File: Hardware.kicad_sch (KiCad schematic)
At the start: 56 parts, among them J1 Conn_01x06_Socket, J2 Micro_SD_Card_Det1, Q1 BC849, Q2 BC849, SW1 Push_Button, SW2 Push_Button, U1 ESP32-WROOM-32, U2 LD1117S33TR_SOT223, U3 SN65HVD231, U4 74LVC125, U5 AMS1117CD-5.0, U6 AMS1117CD-3.3, U7 NEO-M8M, U8 LD1117S33TR_SOT223, U9 AT24CS01-XHM

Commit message: mostly finisged scematics
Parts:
- added AE2, AE3: Antenna_Shield, symbol Device:Antenna_Shield
- added C18, C21, C24: C, symbol Device:C
- added C19, C32, C33, C34: 0.1uF, symbol Device:C
- added C20: 0.1uF, Capacitor_SMD:C_0805_2012Metric_Pad1.18x1.45mm_HandSolder, symbol Device:C_Small
- added C25: 22pF, symbol Device:C
- added C26, C30: 100uF, symbol Device:C
- added C31: 1uF, symbol Device:C
- added D4: ESDA5V3SC5, Package_TO_SOT_SMD:SOT-23-5, symbol Power_Protection:ESDA5V3SC5
- added D5: BSD3C051V, Diode_SMD:D_SOD-323, symbol Device:D_TVS
- added D6, D7: LED, symbol Device:LED
- added D8: BAT54W, Package_TO_SOT_SMD:SOT-323_SC-70, symbol Diode:BAT54W
- added J3: SIM_Card_Shielded, symbol Connector:SIM_Card_Shielded
- added J5: USB_C_Receptacle_USB2.0_14P, symbol Connector:USB_C_Receptacle_USB2.0_14P
- added JP1: SolderJumper_2_Open, symbol Jumper:SolderJumper_2_Open
- added JP2: Jumper_2_Open, symbol Jumper:Jumper_2_Open
- added L2: BLM15PX121SN1D, Inductor_SMD:L_0402_1005Metric, symbol Device:L_Small
- added L3: blm18bb121sn1d, symbol Device:L_Ferrite
- added Q3, Q4, Q6: DTC143Z, symbol Transistor_BJT:DTC143Z
- added Q5: FDN340P, Package_TO_SOT_SMD:SOT-23, symbol Transistor_FET:FDN340P
- added R13: 1M, Resistor_SMD:R_1206_3216Metric_Pad1.30x1.75mm_HandSolder, symbol Device:R_Small
- added R14, R15: 5.1k, Resistor_SMD:R_1206_3216Metric_Pad1.30x1.75mm_HandSolder, symbol Device:R_Small
- added R16: 0R, symbol Device:R
- added R17, R18, R19, R20: R, symbol Device:R
- added U10: SIM7080G, SIM7080G:XCVR_SIM7080G, symbol SIM7080G:SIM7080G
- added U11: TXB0104PW, Package_SO:TSSOP-14_4.4x5mm_P0.65mm, symbol Logic_LevelTranslator:TXB0104PW
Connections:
- net 3.3V: now also C33.1, Q5.2 (S), R20.1, U10.34 (VBAT), U10.35 (VBAT), U11.14 (VCCB)
- net DTR: now also U11.3 (A2)
- net GND: now also AE2.2 (Shield), AE3.2 (Shield), C18.2, C19.2, C20.1, C21.2, C24.2, C26.2, C30.2, C31.2, C32.2, C33.2, C34.1, D4.2 (A), D5.2 (A2), J3.5 (GND), J3.SH, J5.S1 (SHIELD), JP2.1 (A), L2.2, Q3.2 (E), Q4.2 (E), Q6.2 (E), R13.1, U10.13 (GND), U10.19 (GND), U10.21 (GND), U10.27 (GND), U10.30 (GND), U10.31 (GND), U10.33 (GND), U10.36 (GND), U10.37 (GND), U10.45 (GND), U10.63 (GND), U10.66 (GND), U10.67 (GND), U10.69 (GND), U10.70 (GND), U10.71 (GND), U10.72 (GND), U10.73 (GND), U10.74 (GND), U10.75 (GND), U10.76 (GND), U10.77 (GND), U10.8 (GND), U11.7 (GND)
- new net: C21.1, R16.1, U10.32 (RF_ANT)
- new net: D8.1 (A), JP2.2 (B), U10.39 (PWRKEY)
- new net: J5.A5 (CC1), R14.1
- new net: JP1.1 (A), R19.2
- new net: AE2.1 (A), C24.1, R16.2
- new net: D7.1 (K), Q4.3 (C)
- new net: D7.2 (A), R18.2
- new net: Q5.1 (G), Q6.3 (C), R20.2
- new net: L3.2, Q5.3 (D)
- new net: J5.B5 (CC2), R15.1
- new net: D6.2 (A), R17.2
- new net: JP1.2 (B), U10.20 (USB_BOOT)
- new net: C25.2, U10.68 (GNSS_ANT)
- new net: D6.1 (K), Q3.3 (C)
- new net 1.8V: C34.2, R19.1, U10.40 (VDD_EXT), U11.1 (VCCA), U11.8 (OE)
- new net ANT_CTRL: Q6.1 (B)
- new net GNDPWR: C20.2, D5.1 (A1), J5.A1 (GND), J5.A12 (GND), J5.B1 (GND), J5.B12 (GND), L2.1, R13.2, R14.2, R15.2
- new net NB_RI: U10.7 (UART1_RI), U11.13 (B1)
- new net NB_RXD: U10.2 (UART1_RXD), U11.11 (B3)
- new net NB_TXD: U10.1 (UART1_TXD), U11.10 (B4)
- new net ND_DTR: U10.6 (UART1_DTR), U11.12 (B2)
- new net NETLIGHT: Q4.1 (B), U10.41 (NETLIGHT)
- new net PWRKEY: D8.3 (K)
- new net RI: U11.2 (A1)
- new net RXD: U11.4 (A3)
- new net SIM_CLK: D4.1 (K), J3.3 (CLK), U10.16 (SIM_CLK)
- new net SIM_DATA: D4.3 (K), J3.7 (I/O), U10.15 (SIM_DATA)
- new net SIM_RST: D4.4 (K), J3.2 (RST), U10.17 (SIM_RST)
- new net SIM_VDD: C18.1, D4.5 (K), J3.1 (VCC), U10.18 (SIM_VDD)
- new net STAT: Q3.1 (B), U10.42 (STATUS)
- new net TXD: U11.5 (A4)
- new net USB D+: J5.A6 (D+), J5.B6 (D+), U10.25 (USB_DP)
- new net USB D-: J5.A7 (D-), J5.B7 (D-), U10.26 (USB_DM)
- new net VANT: AE3.1 (A), C25.1, L3.1
- new net VBAT: C26.1, C30.1, C31.1, C32.1, R17.1, R18.1
- new net VBUS: C19.1, J5.A4 (VBUS), J5.A9 (VBUS), J5.B4 (VBUS), J5.B9 (VBUS), U10.24 (USB_VBUS)
- no-connect marks 33 -> 60
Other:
- note added: "LTE"
- moved on the sheet: AE1, BT1, C10, C11, C12, C13, C14, C15, C16, C17, C2, C22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

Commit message: done some layouting
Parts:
- removed C10, C15, C2, C3: 100nF, symbol Device:C
- removed C11, C12, C16, C8: 10uF, Capacitor_SMD:C_1206_3216Metric_Pad1.33x1.80mm_HandSolder, symbol Device:C
- removed C13, C14, C17, C9: 4.7uF, symbol Device:C
- removed U2, U8: LD1117S33TR_SOT223, Package_TO_SOT_SMD:SOT-223-3_TabPin2, symbol Regulator_Linear:LD1117S33TR_SOT223
- removed U5: AMS1117CD-5.0, Package_TO_SOT_SMD:TO-252-3_TabPin2, symbol Regulator_Linear:AMS1117CD-5.0
- removed U6: AMS1117CD-3.3, Package_TO_SOT_SMD:TO-252-3_TabPin2, symbol Regulator_Linear:AMS1117CD-3.3
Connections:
- net 3.3v is gone; now on net +3.3V: D2.2 (A), U7.23 (VCC), U9.8 (VCC)
- net CanH_Out is gone; now on net CanH: C27.2, D3.2, L4.3, R10.2
- net CanL_Out is gone; now on net CanL: C29.2, D3.1, L4.4, R11.2
- net Gps_RX is gone; now on net GPS_RX: U7.21 (RXD/SPI_MOSI)
- net Gps_TX is gone; now on net GPS_TX: U7.20 (TXD/SPI_MISO)
- net RXD is gone; now on net LTE_RX: U11.4 (A3)
- net TXD is gone; now on net LTE_TX: U11.5 (A4)
- net VBAT is gone; now on net +3.3V: C26.1, C30.1, C31.1, C32.1, R17.1, R18.1
- net ANT_CTRL: now also U1.11 (IO26)
- net CanH: no longer L4.2, U3.7 (CANH)
- net CanL: no longer L4.1, U3.6 (CANL)
- net PWRKEY: now also U1.10 (IO25)
- net LTE_RX: now reaches U1.16 (IO13)
- net LTE_TX: now reaches U1.27 (IO16)
- net GPS_RX: now reaches U1.28 (IO17)
- net GPS_TX: now reaches U1.33 (IO21)
- net 3.3V renamed +3.3V
- net CS_SD renamed SD_CS
- net Gps_SCL renamed GPS_SCL
- net Gps_SDA renamed GPS_SDA
- net RX renamed PROG_RX
- net RxCan renamed CAN_RX
- net TX renamed PROG_TX
- net TxCan renamed CAN_TX
- new net CanH_Int: L4.2, U3.7 (CANH)
- new net CanL_Int: L4.1, U3.6 (CANL)
- no-connect marks 60 -> 55
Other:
- note added: "GSM antenna controll"
- note added: "LTE Info Leds"
- note added: "LTE Module"
- note added: "LTE Usb"
- note added: "Levelshifter for LTE"
- note added: "SIM Card"
- note removed: "LTE"
- note removed: "Voltage Converter"
- moved on the sheet: AE2, AE3, BT1, C1, C18, C19, C20, C21, C22, C23, C24, C25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

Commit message: added testpoints
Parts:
- added H1, H2, H3, H4, H5, H6, H7, H8: MountingHole_Pad, symbol Mechanical:MountingHole_Pad
- added TP1, TP10, TP11, TP12, TP13, TP14, TP15, TP16, TP17, TP3, TP4, TP5, TP6, TP7, TP8, TP9: TestPoint, symbol Connector:TestPoint
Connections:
- net +3.3V: now also TP4.1
- net +3V3: now also TP17.1
- net ANT_CTRL: now also TP10.1
- net CAN_RX: now also TP14.1
- net CAN_TX: now also TP13.1
- net CanH_Int: now also TP12.1
- net CanL_Int: now also TP11.1
- net EN: now also TP15.1
- net GND: now also H1.1, H2.1, H3.1, H4.1, H5.1, H6.1, H7.1, H8.1
- net IO0: now also TP16.1
- net NETLIGHT: now also TP8.1
- net STAT: now also TP9.1
- net USB D+: now also TP7.1
- net USB D-: now also TP6.1
- net VANT: now also TP3.1
- net at D8.1 (A), JP2.2 (B), U10.39 (PWRKEY): now also TP5.1
- no-connect marks 55 -> 53
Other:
- note added: "Mounting"
- moved on the sheet: AE2, AE3, C1, C19, C21, C24, C25, C26, C27, C28, C29, C30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

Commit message: moved everythint into hirachical sheets
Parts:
- removed AE1: Antenna, symbol Device:Antenna
- removed AE2, AE3: Antenna_Shield, symbol Device:Antenna_Shield
- removed BT1: Battery_Cell, symbol Device:Battery_Cell
- removed C18, C21, C24: C, symbol Device:C
- removed C19, C32, C33, C34: 0.1uF, symbol Device:C
- removed C20: 0.1uF, Capacitor_SMD:C_0805_2012Metric_Pad1.18x1.45mm_HandSolder, symbol Device:C_Small
- removed C25: 22pF, symbol Device:C
- removed C26, C30: 100uF, symbol Device:C
- removed C27, C29: 100pF, Capacitor_SMD:C_0805_2012Metric_Pad1.18x1.45mm_HandSolder, symbol Device:C
- removed C28: 4nF, Capacitor_SMD:C_0805_2012Metric_Pad1.18x1.45mm_HandSolder, symbol Device:C
- removed C31: 1uF, symbol Device:C
- removed C6: 22uF, Capacitor_SMD:C_1206_3216Metric_Pad1.33x1.80mm_HandSolder, symbol Device:C
- removed C7: 0.1uF, Capacitor_SMD:C_0805_2012Metric_Pad1.18x1.45mm_HandSolder, symbol Device:C
- removed D1, D6, D7: LED, symbol Device:LED
- removed D2: D, symbol Device:D
- removed D3: PESD1CAN, Package_TO_SOT_SMD:SOT-23-3, symbol PESD1CAN:PESD1CAN
- removed D4: ESDA5V3SC5, Package_TO_SOT_SMD:SOT-23-5, symbol Power_Protection:ESDA5V3SC5
- removed D5: BSD3C051V, Diode_SMD:D_SOD-323, symbol Device:D_TVS
- removed D8: BAT54W, Package_TO_SOT_SMD:SOT-323_SC-70, symbol Diode:BAT54W
- removed H5, H6, H7, H8: MountingHole_Pad, symbol Mechanical:MountingHole_Pad
- removed J2: Micro_SD_Card_Det1, symbol Connector:Micro_SD_Card_Det1
- removed J3: SIM_Card_Shielded, symbol Connector:SIM_Card_Shielded
- removed J5: USB_C_Receptacle_USB2.0_14P, symbol Connector:USB_C_Receptacle_USB2.0_14P
- removed JP1: SolderJumper_2_Open, symbol Jumper:SolderJumper_2_Open
- removed JP2: Jumper_2_Open, symbol Jumper:Jumper_2_Open
- removed L1: 27uH, symbol Device:L
- removed L2: BLM15PX121SN1D, Inductor_SMD:L_0402_1005Metric, symbol Device:L_Small
- removed L3: blm18bb121sn1d, symbol Device:L_Ferrite
- removed L4: EPCO B82787C0513, footprints:EPCO B82787C0513, symbol Device:L_Ferrite_Coupled_Small_1423
- removed Q3, Q4, Q6: DTC143Z, symbol Transistor_BJT:DTC143Z
- removed Q5: FDN340P, Package_TO_SOT_SMD:SOT-23, symbol Transistor_FET:FDN340P
- removed R10, R11: 60R, Resistor_SMD:R_1206_3216Metric_Pad1.30x1.75mm_HandSolder, symbol Device:R
- removed R12, R17, R18, R19, R20: R, symbol Device:R
- removed R13: 1M, Resistor_SMD:R_1206_3216Metric_Pad1.30x1.75mm_HandSolder, symbol Device:R_Small
- removed R14, R15: 5.1k, Resistor_SMD:R_1206_3216Metric_Pad1.30x1.75mm_HandSolder, symbol Device:R_Small
- removed R16: 0R, symbol Device:R
- removed R2, R5, R6, R7: 3.3K, symbol Device:R
- removed R8: 22R, symbol Device:R
- removed R9: 1k, symbol Device:R
- removed TP1, TP10, TP11, TP12, TP13, TP14, TP3, TP4, TP5, TP6, TP7, TP8, TP9: TestPoint, symbol Connector:TestPoint
- removed U10: SIM7080G, SIM7080G:XCVR_SIM7080G, symbol SIM7080G:SIM7080G
- removed U11: TXB0104PW, Package_SO:TSSOP-14_4.4x5mm_P0.65mm, symbol Logic_LevelTranslator:TXB0104PW
- removed U3: SN65HVD231, Package_SO:SOIC-8_3.9x4.9mm_P1.27mm, symbol Interface_CAN_LIN:SN65HVD231
- removed U4: 74LVC125, symbol 74xx:74LVC125
- removed U7: NEO-M8M, RF_GPS:ublox_NEO, symbol RF_GPS:NEO-M8M
- removed U9: AT24CS01-XHM, Package_SO:TSSOP-8_4.4x3mm_P0.65mm, symbol Memory_EEPROM:AT24CS01-XHM
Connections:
- net RTS is gone; now on net DTR: Q1.2 (E), R4.1
- no-connect marks 53 -> 19
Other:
- added sheet CAN_Module (CAN_Module.kicad_sch)
- added sheet GPS_Module (GPS_Modula.kicad_sch)
- added sheet LTE_Module (LTE_Module.kicad_sch)
- added sheet SD_Modula (SD_Modula.kicad_sch)
- note removed: "Can Protection"
- note removed: "Can Trancever"
- note removed: "GPS"
- note removed: "GSM antenna controll"
- note removed: "LTE Info Leds"
- note removed: "LTE Module"
- note removed: "LTE Usb"
- note removed: "Levelshifter for LTE"
- note removed: "SD Reader"
- note removed: "SIM Card"
- moved on the sheet: C22, C23, H1, H2, H3, H4, J1, Q1, Q2, R3, R4, SW1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

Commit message: fixed layout
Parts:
- added TP13, TP14: TestPoint, symbol Connector:TestPoint
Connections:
- net DTR: now also J1.2 (Pin_2), J1.6 (Pin_6)
- net PROG_RX: now also TP14.1
- net PROG_TX: now also TP13.1
- no-connect marks 19 -> 17
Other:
- moved on the sheet: C22, C23, H1, H2, H3, H4, J1, Q1, Q2, R3, R4, SW1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

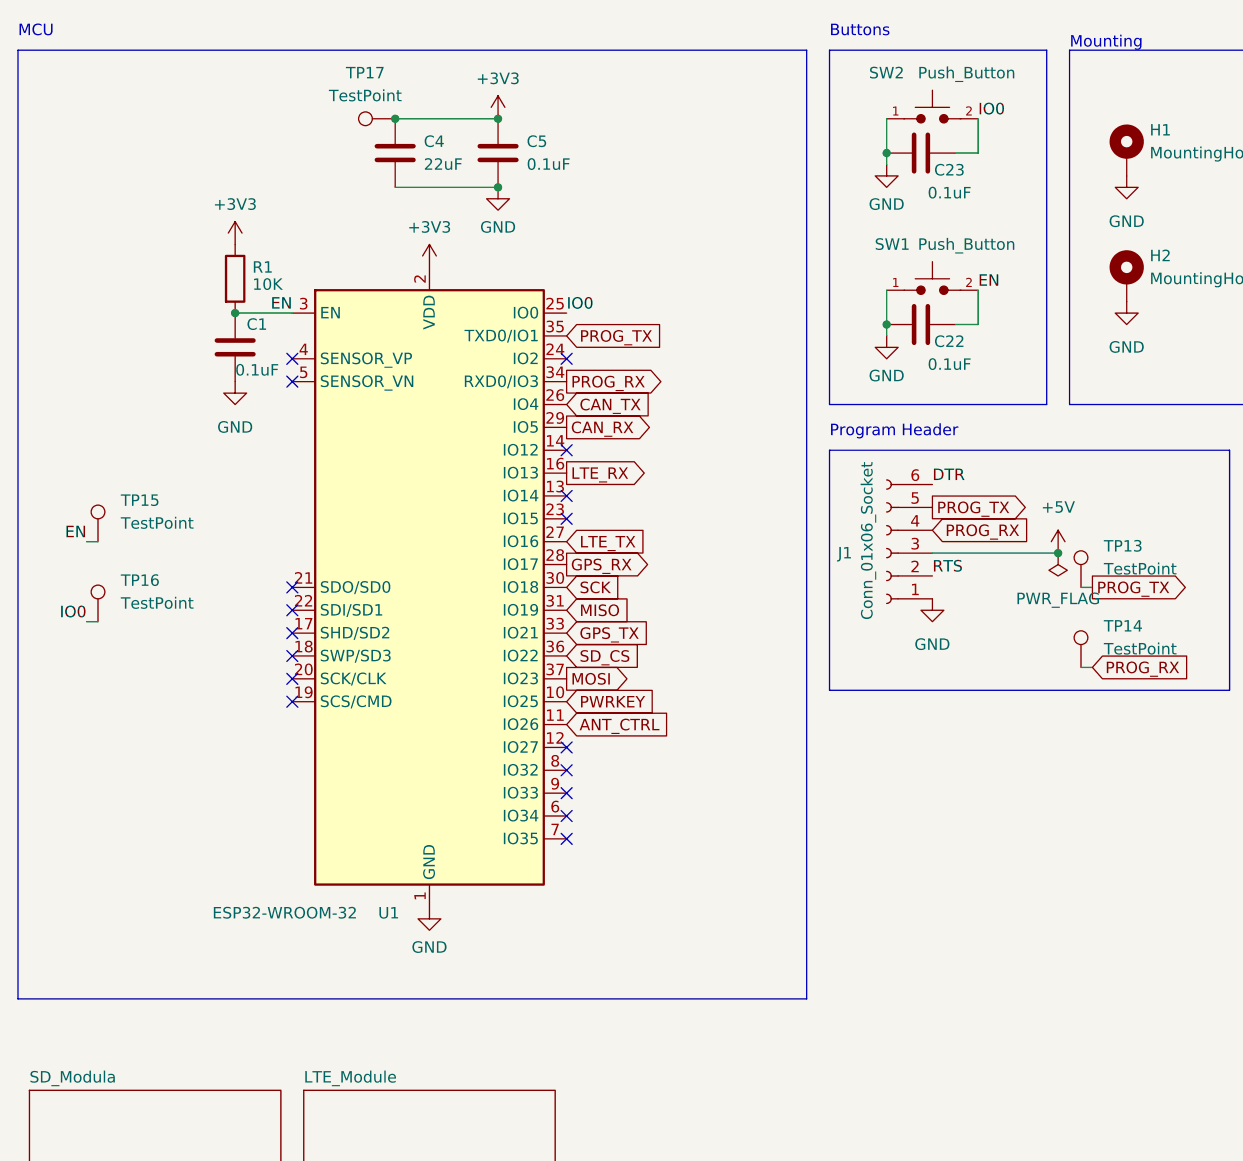
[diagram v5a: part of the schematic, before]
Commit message: added psu and formated board outline
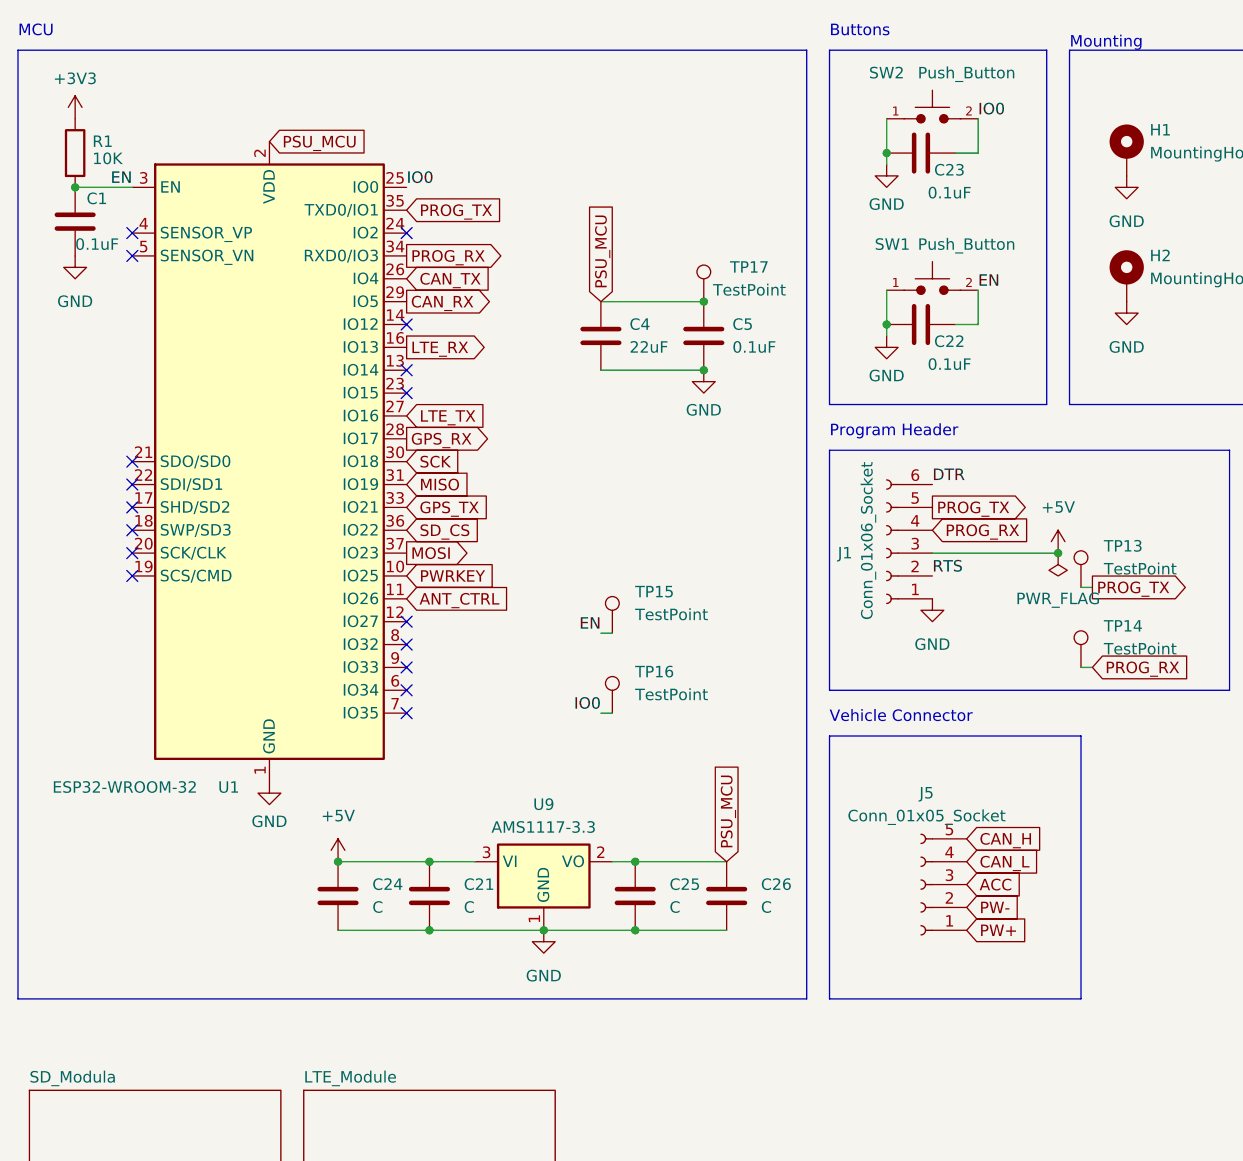
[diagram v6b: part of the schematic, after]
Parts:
- added C21, C24, C25, C26: C, symbol Device:C
- added J5: Conn_01x05_Socket, symbol Connector:Conn_01x05_Socket
- added U9: AMS1117-3.3, Package_TO_SOT_SMD:SOT-223-3_TabPin2, symbol Regulator_Linear:AMS1117-3.3
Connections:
- net +3V3: no longer C4.1, C5.1, TP17.1, U1.2 (VDD)
- net +5V: now also C21.1, C24.1, U9.3 (VI)
- net GND: now also C21.2, C24.2, C25.2, C26.2, U9.1 (GND)
- new net ACC: J5.3 (Pin_3)
- new net CAN_H: J5.5 (Pin_5)
- new net CAN_L: J5.4 (Pin_4)
- new net PSU_MCU: C25.1, C26.1, C4.1, C5.1, TP17.1, U1.2 (VDD), U9.2 (VO)
- new net PW+: J5.1 (Pin_1)
- new net PW-: J5.2 (Pin_2)
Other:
- note added: "Vehicle Connector"
- moved on the sheet: C1, C4, C5, R1, TP15, TP16, TP17, U1

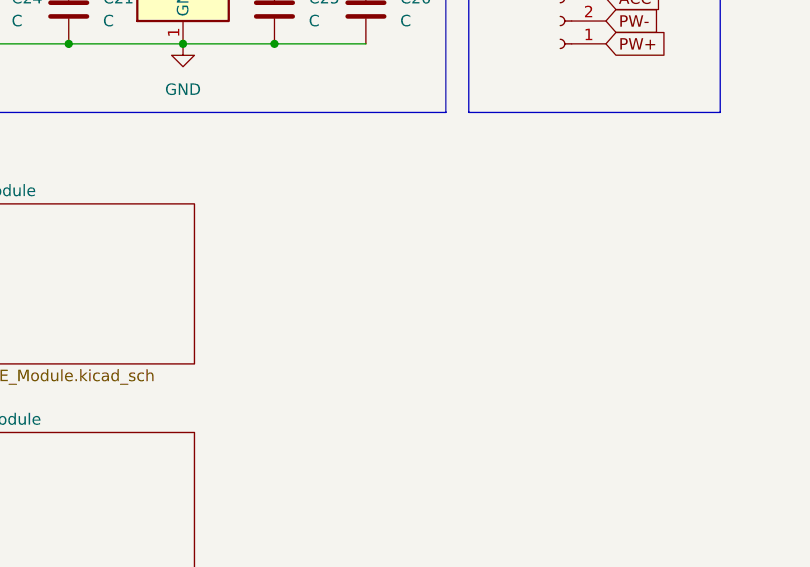
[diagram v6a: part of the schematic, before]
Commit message: added charging footprint
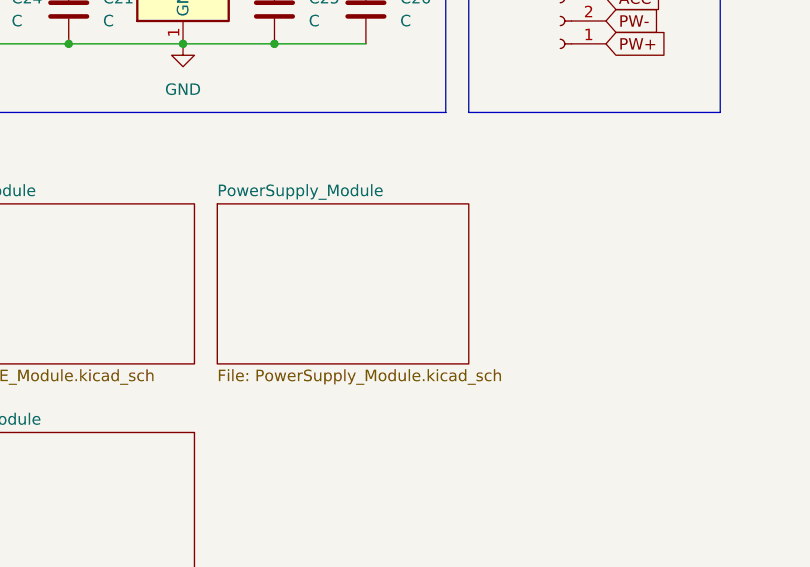
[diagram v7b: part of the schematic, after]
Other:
- added sheet PowerSupply_Module (PowerSupply_Module.kicad_sch)
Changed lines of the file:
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@@
+	)
+	(sheet
+		(at 78.74 133.35)
+		(size 27.94 17.78)
+		(fields_autoplaced yes)
+		(stroke
+			(width 0.1524)
+			(type solid)
+		)
+		(fill
+			(color 0 0 0 0.0000)
+		)
+		(property "Sheetname" "PowerSupply_Module"
+			(at 78.74 132.6384 0)
+			(effects
+				(font
+					(size 1.27 1.27)
+				)
+				(justify left bottom)
+			)
+		)
+		(property "Sheetfile" "PowerSupply_Module.kicad_sch"
+			(at 78.74 151.7146 0)
+			(effects
+				(font
+					(size 1.27 1.27)
+				)
+				(justify left top)
+			)
+		)
+		(instances
+			(project "Hardware"
+				(path "/f04ee758-a926-48b7-b458-286a696c3ef4"
+					(page "6")
+				)
+			)
+		)
 	)
 	(sheet
